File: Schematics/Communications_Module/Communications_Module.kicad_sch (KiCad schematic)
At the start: 77 parts, among them J2 SWD_01x04_Pin, J3 Stack Male Edge Connector, J4 USB_C_Female_USB2_Small, SW1 SW_STM_RESET, SW2 SW_STM_BOOT_MODE, U1 LoRa1262F30, U10 LM66100DCKR, U10 TPM8837C-SO1R, U11 LM66100DCKR, U12 AMS1117-3.3, U2 W25Q128JVS, U4 LM66100DCKR, U5 LM66100DCKR, U6 LM66100DCKR, U7 STM32F103CBT6, U8 CP2102N-Axx-xQFN28, U9 ISO1042BDWVR, Y1 X322516MMB4SI

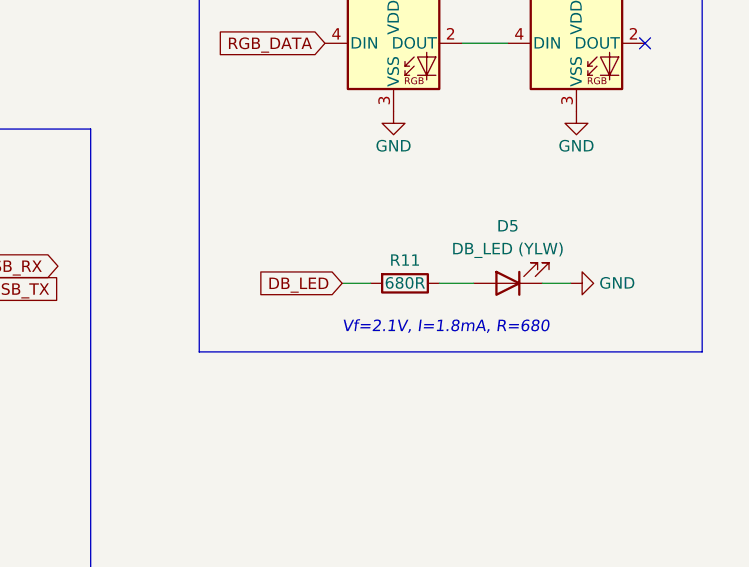
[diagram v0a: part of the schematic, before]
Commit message: update datasheet referencing
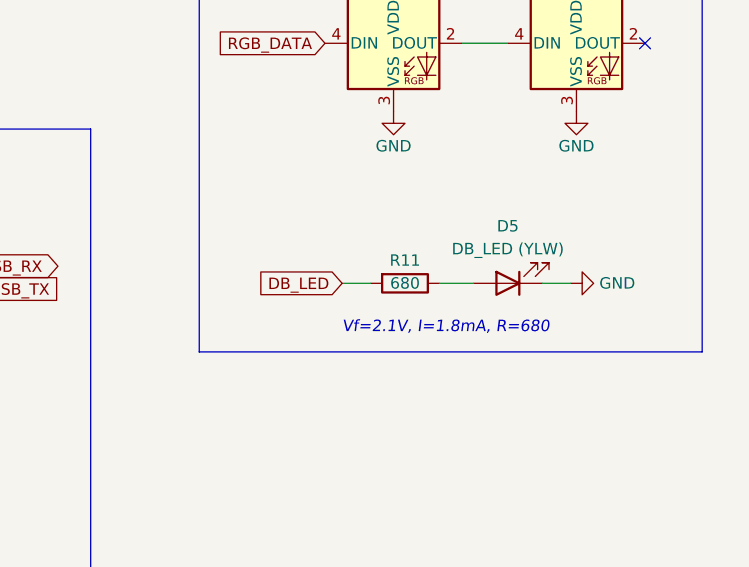
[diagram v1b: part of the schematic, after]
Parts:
- R11: value 680R -> 680
- U1: Datasheets2 (none) -> ${KIPRJMOD}/../../Datasheets/DS_SX1261-2_V1.2.pdf
